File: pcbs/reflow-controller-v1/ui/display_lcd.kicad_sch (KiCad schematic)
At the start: 1 part

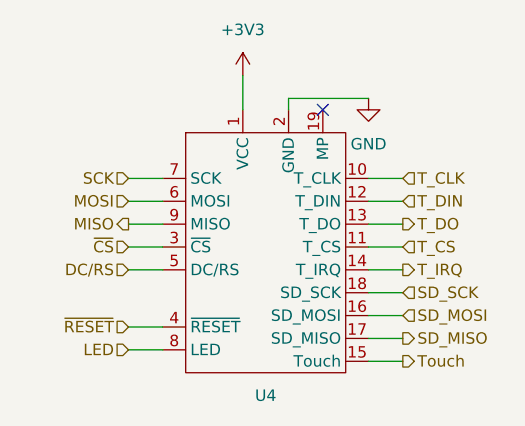
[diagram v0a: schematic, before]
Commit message: split pcbs into two for safety
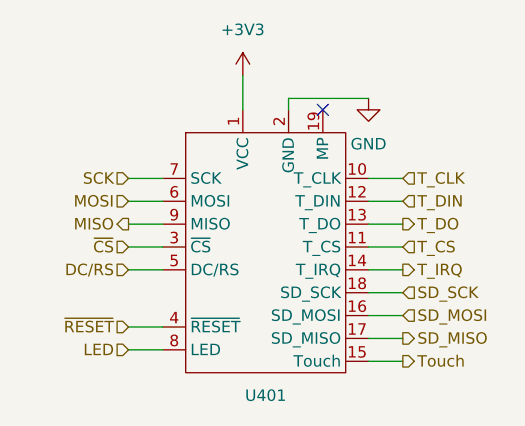
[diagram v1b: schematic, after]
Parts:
- renumbered U4 to U401
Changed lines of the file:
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@@
 (kicad_sch
-	(version 20231120)
+	(version 20250114)
 	(generator "eeschema")
-	(generator_version "8.0")
+	(generator_version "9.0")
 	(paper "A4")
 	(no_connect
@@
 		(shape output)
 		(at 151.13 101.6 0)
-		(fields_autoplaced yes)
 		(effects
 			(font
@@
 		(shape input)
 		(at 120.65 100.33 180)
-		(fields_autoplaced yes)
 		(effects
 			(font
@@
 		(shape input)
 		(at 120.65 93.98 180)
-		(fields_autoplaced yes)
 		(effects
 			(font
@@
 		(shape output)
 		(at 120.65 88.9 180)
-		(fields_autoplaced yes)
 		(effects
 			(font
@@
 		(shape input)
 		(at 120.65 91.44 180)
-		(fields_autoplaced yes)
 		(effects
 			(font
@@
 		(shape output)
 		(at 151.13 88.9 0)
-		(fields_autoplaced yes)
 		(effects
 			(font
@@
 		(shape output)
 		(at 151.13 93.98 0)
-		(fields_autoplaced yes)
 		(effects
 			(font
@@
 		(shape input)
 		(at 120.65 86.36 180)
-		(fields_autoplaced yes)
 		(effects
 			(font
@@
 		(shape input)
 		(at 120.65 83.82 180)
-		(fields_autoplaced yes)
 		(effects
 			(font
@@
 		(shape input)
 		(at 151.13 86.36 0)
-		(fields_autoplaced yes)
 		(effects
 			(font
@@
 		(shape input)
 		(at 151.13 83.82 0)
-		(fields_autoplaced yes)
 		(effects
 			(font
@@
 		(shape input)
 		(at 151.13 99.06 0)
-		(fields_autoplaced yes)
 		(effects
 			(font
@@
 		(shape input)
 		(at 151.13 91.44 0)
-		(fields_autoplaced yes)
 		(effects
 			(font
@@
 		(shape input)
 		(at 120.65 102.87 180)
-		(fields_autoplaced yes)
 		(effects
 			(font
@@
 		(shape input)
 		(at 151.13 96.52 0)
-		(fields_autoplaced yes)
 		(effects
 			(font
@@
 		(shape output)
 		(at 151.13 104.14 0)
-		(fields_autoplaced yes)
 		(effects
 			(font
@@
 		(dnp no)
 		(fields_autoplaced yes)
-		(property "Reference" "U4"
+		(property "Reference" "U401"
 			(at 135.89 107.95 0)
 			(effects
@@
 		)
 		(instances
-			(project ""
-				(path "/843848ae-bf49-42cb-8f8b-76790d2e568d/f628d05d-4e2a-4195-9ee3-f88b775e9255"
-					(reference "U4")
+			(project "ui"
+				(path "/2ced3b3e-2fc8-4776-88d1-4bcb3cd16514/3002f892-b564-4483-ae2b-de535155d456"
+					(reference "U401")
 					(unit 1)
 				)
@@
 		(dnp no)
 		(fields_autoplaced yes)
-		(property "Reference" "#PWR0702"
+		(property "Reference" "#PWR0402"
 			(at 147.32 81.28 0)
 			(effects
@@
 		)
 		(instances
-			(project "reflow-controller-v1"
-				(path "/843848ae-bf49-42cb-8f8b-76790d2e568d/f628d05d-4e2a-4195-9ee3-f88b775e9255"
-					(reference "#PWR0702")
+			(project "ui"
+				(path "/2ced3b3e-2fc8-4776-88d1-4bcb3cd16514/3002f892-b564-4483-ae2b-de535155d456"
+					(reference "#PWR0402")
 					(unit 1)
 				)
@@
 		(dnp no)
 		(fields_autoplaced yes)
-		(property "Reference" "#PWR0701"
+		(property "Reference" "#PWR0401"
 			(at 133.35 76.2 0)
 			(effects
@@
 		)
 		(instances
-			(project "reflow-controller-v1"
-				(path "/843848ae-bf49-42cb-8f8b-76790d2e568d/f628d05d-4e2a-4195-9ee3-f88b775e9255"
-					(reference "#PWR0701")
+			(project "ui"
+				(path "/2ced3b3e-2fc8-4776-88d1-4bcb3cd16514/3002f892-b564-4483-ae2b-de535155d456"
+					(reference "#PWR0401")
 					(unit 1)
 				)
